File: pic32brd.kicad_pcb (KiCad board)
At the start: 2 copper layers, 2 parts, among them IC1 PIC32MX2xx/1xx

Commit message: rev A
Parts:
- added C1: 100n, Capacitors_SMD:C_0805_HandSoldering, B.Cu at (132.1, 57.0)
- added C10: 100n, Capacitors_SMD:C_0805_HandSoldering, B.Cu at (127.0, 36.2)
- added C2: 4.7u, Capacitors_SMD:C_0805_HandSoldering, B.Cu at (128.9, 57.0)
- added C3: 100n, Capacitors_SMD:C_0805_HandSoldering, F.Cu at (135.3, 60.3)
- added C4: 10u, Capacitors_SMD:C_0805_HandSoldering, B.Cu at (130.7, 44.5)
- added C6: 4.7u, Capacitors_SMD:C_0805_HandSoldering, B.Cu at (119.4, 59.7)
- added C7: 10u, Capacitors_SMD:C_0805_HandSoldering, F.Cu at (124.5, 59.7)
- added C8: 100n, Capacitors_SMD:C_0805_HandSoldering, B.Cu at (122.7, 38.0)
- added C9: 100n, Capacitors_SMD:C_0805_HandSoldering, B.Cu at (130.7, 39.5)
- added Con1: prog_header, RS_footprints:Pin_Header_Staggered_1x06, F.Cu at (120.5, 31.1)
- added D1: TX, LEDs:LED_0805, F.Cu at (130.8, 50.2)
- added D2: RX, LEDs:LED_0805, F.Cu at (128.3, 50.2)
- added D3: PWR, LEDs:LED_0805, F.Cu at (118.7, 65.4)
- added D4: RB5, LEDs:LED_0805, F.Cu at (122.8, 50.6)
- added F1: PTC Fuse, Capacitors_SMD:C_0805_HandSoldering, F.Cu at (121.3, 65.4)
- added IC2: PIC32MX2xx/1xx, Housings_SSOP:SSOP-28_5.3x10.2mm_Pitch0.65mm, F.Cu at (127.0, 39.4)
- added IC3: LM3671, TO_SOT_Packages_SMD:SOT-23-5, F.Cu at (119.4, 59.1)
- added L1: 2.2u, Capacitors_SMD:C_0805_HandSoldering, F.Cu at (122.6, 55.9)
- added P1: USB_OTG, RS_footprints:USB-MICRO-B, F.Cu at (127.0, 67.3)
- added P2: CONN_01X09, Pin_Headers:Pin_Header_Straight_1x09, F.Cu at (118.1, 34.3)
- added P3: CONN_01X09, Pin_Headers:Pin_Header_Straight_1x09, F.Cu at (135.9, 34.3)
- added R2: 270, Resistors_SMD:R_0805_HandSoldering, B.Cu at (128.3, 50.2)
- added R3: 10k, Resistors_SMD:R_0805_HandSoldering, B.Cu at (123.2, 42.5)
- added R4: 1k, Resistors_SMD:R_0805_HandSoldering, B.Cu at (122.6, 35.6)
- added R5: 10, Resistors_SMD:R_0805_HandSoldering, B.Cu at (127.0, 41.9)
- added R6: 270, Resistors_SMD:R_0805_HandSoldering, B.Cu at (118.7, 65.4)
- added R7: 270, Resistors_SMD:R_0805_HandSoldering, B.Cu at (122.8, 50.6)
- IC1: value PIC32MX2xx/1xx -> FT230X; footprint Housings_SSOP:SSOP-28_5.3x10.2mm_Pitch0.65mm -> Housings_SSOP:SSOP-16_3.9x4.9mm_Pitch0.635mm
- R1: value R -> 270; moved to B.Cu
- moved IC1 51.2 mm to (130.2, 57.1)
- moved R1 49.7 mm to (130.8, 50.2)
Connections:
- IC1 pad 1: Net-(IC1-Pad1) -> /FTDI/FTX
- IC1 pad 10: (no net) -> /FTDI/3V3
- IC1 pad 11: (no net) -> /FTDI/3V3
- IC1 pad 12: (no net) -> /FTDI/5V0
- IC1 pad 13: (no net) -> /FTDI/GND
- IC1 pad 14: (no net) -> /FTDI/TXLED
- IC1 pad 15: (no net) -> Net-(IC1-Pad15)
- IC1 pad 16: (no net) -> Net-(IC1-Pad16)
- IC1 pad 3: (no net) -> /FTDI/3V3
- IC1 pad 4: (no net) -> /FTDI/FRX
- IC1 pad 5: (no net) -> /FTDI/GND
- IC1 pad 6: (no net) -> Net-(IC1-Pad6)
- IC1 pad 7: (no net) -> /FTDI/RXLED
- IC1 pad 8: (no net) -> /FTDI/USBD+
- IC1 pad 9: (no net) -> /FTDI/USBD-
- R1 pad 1: +3V3 -> Net-(D1-Pad1)
- R1 pad 2: Net-(IC1-Pad1) -> /FTDI/TXLED
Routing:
- net /SWREG_5to3V3/3V3: track 0.00 -> 82.6 mm, vias 0 -> 4
- net /FTDI/5V0: track 0.00 -> 46.7 mm, vias 0 -> 4
- net /FTDI/3V3: track 0.00 -> 20.2 mm
- net /FTDI/FRX: track 0.00 -> 18.7 mm, vias 0 -> 2
- net /FTDI/GND: track 0.00 -> 17.7 mm, vias 0 -> 8
- net /FTDI/FTX: track 0.00 -> 16.6 mm
- net /microcontroller/RB5: track 0.00 -> 15.1 mm
- net /microcontroller/RA3: track 0.00 -> 14.0 mm
- net /microcontroller/RA2: track 0.00 -> 12.1 mm
- net /microcontroller/RB3: track 0.00 -> 11.5 mm
- net /microcontroller/PGC: track 0.00 -> 11.2 mm
- net /microcontroller/~MCLR: track 0.00 -> 10.9 mm
- net /microcontroller/PGD: track 0.00 -> 10.8 mm
- net /FTDI/RXLED: track 0.00 -> 9.92 mm, vias 0 -> 1
- net /microcontroller/RB2: track 0.00 -> 9.55 mm
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- added copper zone on B.Cu, net /FTDI/GND
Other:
- board outline added: 21.6 x 40 mm
- net class Default: clearance 0.2 -> 0.1524; trace_width 0.25 -> 0.1524; via_dia 0.6 -> 0.635; via_drill 0.4 -> 0.3302
- net class Power added: clearance 0.1524, trace_width 0.762, via_dia 0.635, via_drill 0.3302
- net class Signals added: clearance 0.1524, trace_width 0.508, via_dia 0.635, via_drill 0.3302
- rule pad_to_mask_clearance: 0.2 -> 0.0254
- rule trace_clearance: 0.2 -> 0.1524
- rule trace_min: 0.2 -> 0.1524
- rule via_min_drill: 0.3 -> 0.3302
- rule via_min_size: 0.4 -> 0.635
- board text added: "3.3V"
- board text added: "5V"
- board text added: "GND"
- board text added: "James Irwin"
- board text added: "PIC32 Dev Board"
- board text added: "RA0"
- board text added: "RA1"
- board text added: "RA2"
- board text added: "RA3"
- board text added: "RB0"
- board text added: "RB1"
- board text added: "RB13"
- board text added: "RB14"
- board text added: "RB15"
- board text added: "RB2"
- board text added: "RB3"
- board text added: "RB5"
- board text added: "RB7"
- board text added: "RB8"
- board text added: "RB9"
- board text added: "Rev A"

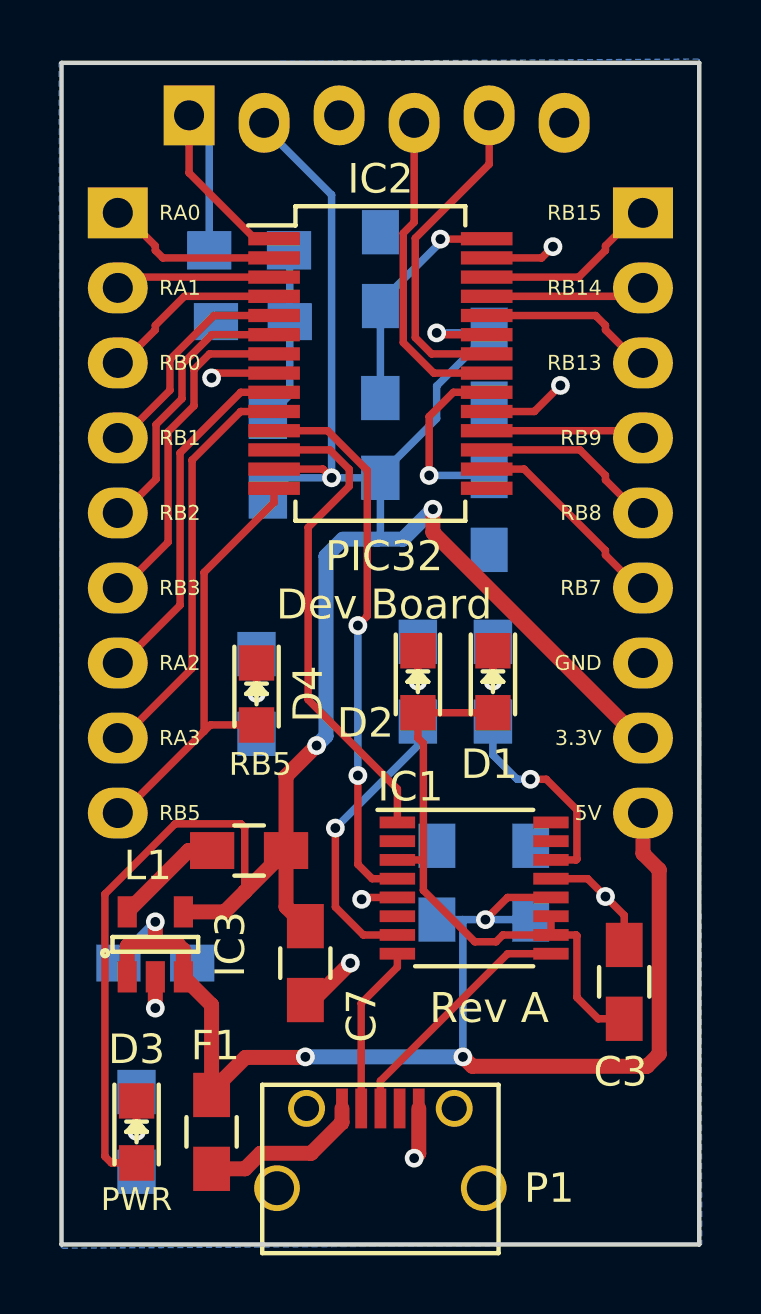
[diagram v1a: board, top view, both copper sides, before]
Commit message: Rev B
added USB termination, swapped D+ and D- lines to be correct, and re-routed the board
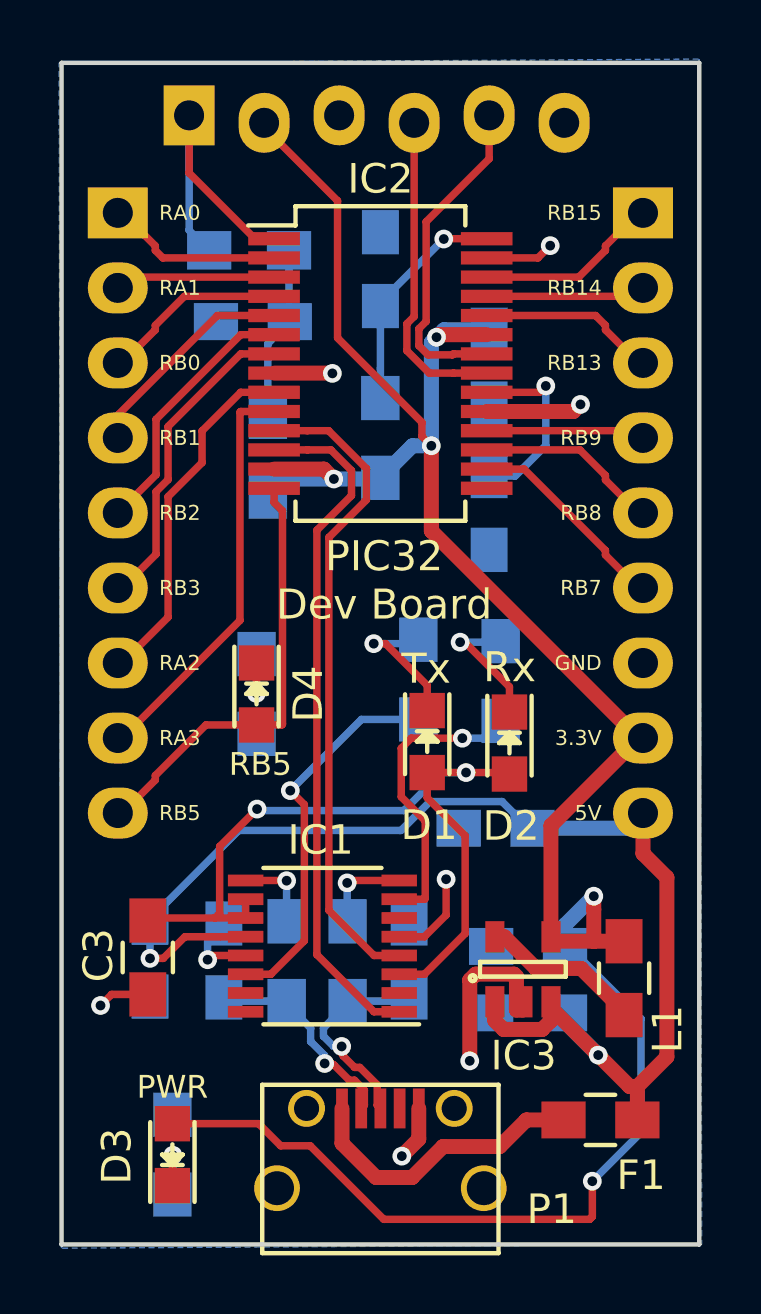
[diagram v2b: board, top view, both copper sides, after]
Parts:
- added C11: 47p, Capacitors_SMD:C_0805_HandSoldering, B.Cu at (128.0, 59.6)
- added C5: 47p, Capacitors_SMD:C_0805_HandSoldering, B.Cu at (121.7, 59.6)
- added R8: 27, Resistors_SMD:R_0805_HandSoldering, B.Cu at (123.8, 59.6)
- added R9: 27, Resistors_SMD:R_0805_HandSoldering, B.Cu at (125.9, 59.6)
- C7: moved to B.Cu
- moved C3 16.2 mm to (119.1, 59.5), turned to 270 degrees
- moved L1 13.4 mm to (135.2, 60.2), turned to 270 degrees
- moved F1 13.2 mm to (134.4, 65.0), turned to 180 degrees
- moved C6 12.7 mm to (132.0, 61.4), turned to 180 degrees
- moved IC3 12.5 mm to (131.8, 59.9)
- moved C2 10.1 mm to (119.2, 59.6), turned to 270 degrees
- moved C7 7.56 mm to (132.0, 59.1), turned to 180 degrees
- moved IC1 5.50 mm to (125.0, 59.1), turned to 180 degrees
- moved D2 3.73 mm to (131.4, 52.2)
- moved D1 3.01 mm to (128.6, 52.2)
- moved R2 2.80 mm to (131.1, 50.1)
- moved R1 2.53 mm to (128.3, 50.1)
- moved C1 2.19 mm to (130.9, 55.1), turned to 180 degrees
- moved D3 1.44 mm to (120.0, 66.2), turned to 90 degrees
- moved R6 1.44 mm to (120.0, 66.2), turned to 90 degrees
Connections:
- net /FTDI/3V3 renamed /FTDI/3V3_IO
- P1 pad 2: /FTDI/USBD+ -> /D-
- P1 pad 3: /FTDI/USBD- -> /D+
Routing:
- net /FTDI/3V3_IO: track 20.2 -> 27.5 mm, vias 0 -> 2
- net /D-: track 0.00 -> 7.21 mm, vias 0 -> 1
- net /D+: track 0.00 -> 7.17 mm, vias 0 -> 1
- net /FTDI/FTX: track 16.6 -> 23.4 mm
- net /FTDI/TXLED: track 7.30 -> 13.1 mm
- net /FTDI/USBD-: track 8.49 -> 2.77 mm, vias 0 -> 1
- net /FTDI/GND: track 17.7 -> 23.1 mm
- net Net-(F1-Pad2): track 5.54 -> 9.97 mm
- net /FTDI/FRX: track 18.7 -> 22.2 mm, vias 2 -> 0
- net /FTDI/USBD+: track 5.74 -> 3.10 mm, vias 0 -> 1
- net Net-(D1-Pad1): track 2.36 -> 4.81 mm
- net /FTDI/5V0: track 46.7 -> 44.5 mm, vias 4 -> 2
- net Net-(D2-Pad1): track 2.36 -> 4.53 mm
- net Net-(IC3-Pad5): track 3.73 -> 5.55 mm
- net /microcontroller/AVDD: track 8.45 -> 7.73 mm
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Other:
- board text added: "Rev B"
- board text added: "Rx"
- board text added: "Tx"
- board text removed: "Rev A"
